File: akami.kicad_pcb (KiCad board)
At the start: 4 copper layers, 30 x 33.3 mm, 66 parts, among them J1 USB_C_Receptacle_USB2.0, J2 Conn_01x01, J3 Conn_01x01, Q2 AO3401A, U1 nRF52840, U2 TP4054, U3 AP2112K-3.3, U4 ProMicro_2, Y1 32MHz, Y2 32.768 kHz

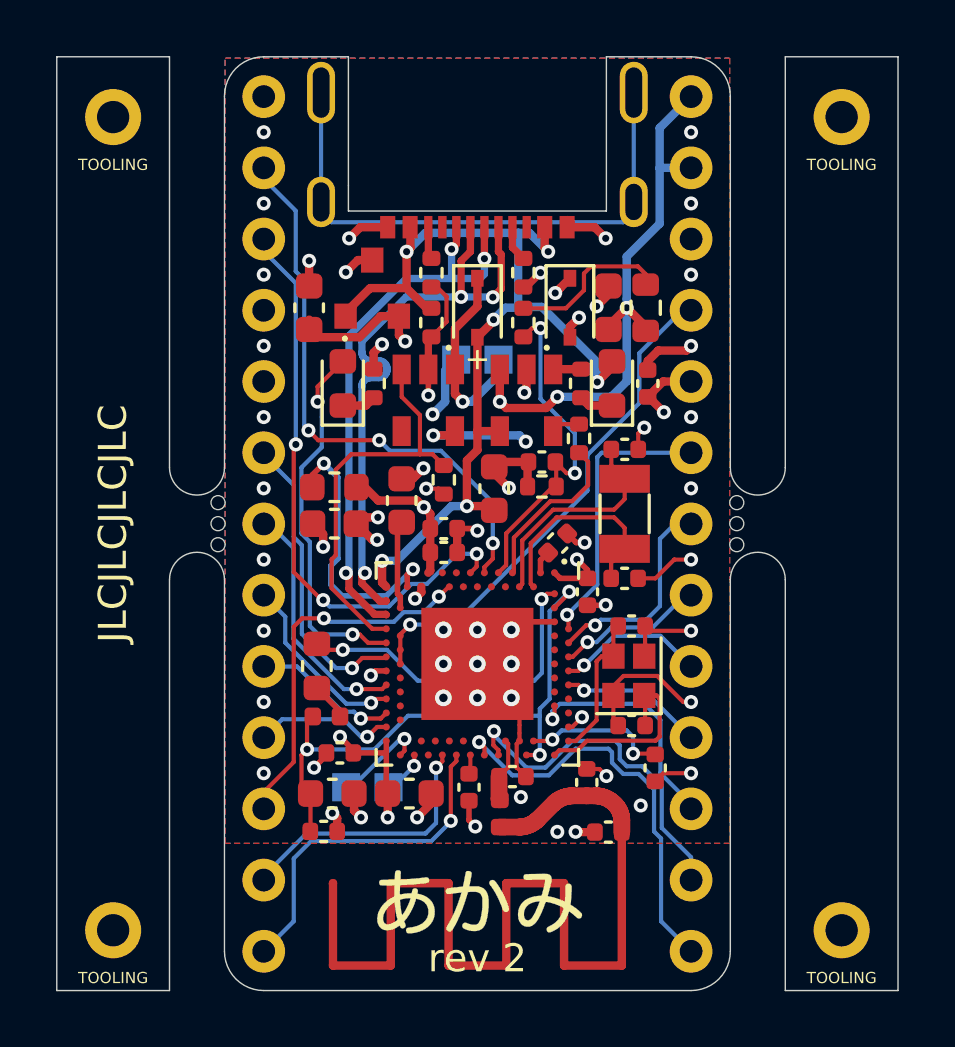
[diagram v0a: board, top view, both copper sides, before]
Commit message: rev 2.1 (hv): 1. remove the 1M pulldown on the LDO enable pin; AP2112K has an    internal pull-down already. 2. adjust pcb layout/routing slightly.
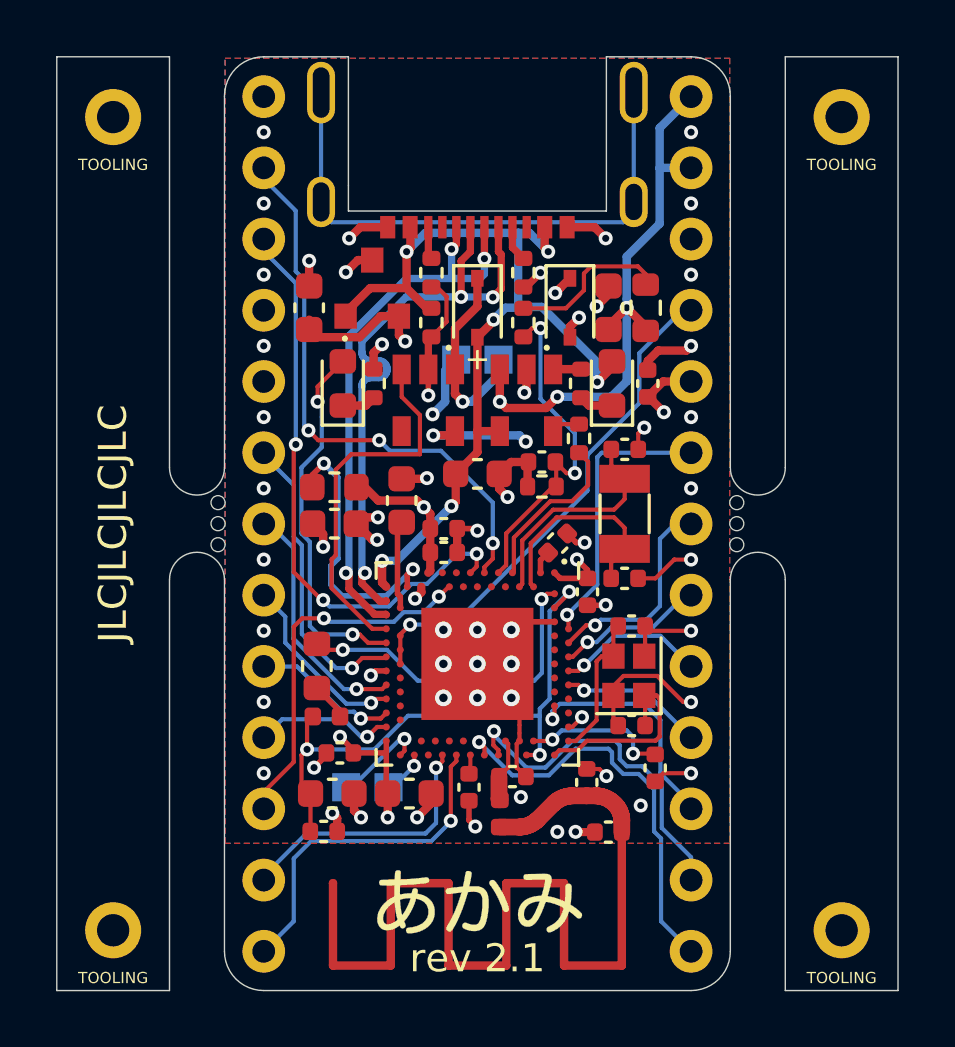
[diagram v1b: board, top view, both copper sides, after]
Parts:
- removed R1: 1M, Resistor_SMD:R_0402_1005Metric
- moved C14 0.80 mm to (0.00, -1.77), turned to 180 degrees
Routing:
- net VBUS: track 35.3 -> 34.0 mm
- net POWER_CTRL: track 14.4 -> 13.4 mm
- net GND: track 43.7 -> 42.8 mm, vias 55 -> 54
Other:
- board text added: "rev 2.1"
- board text removed: "rev 2"

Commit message: rev 2.2 (hv): 1. remove the diode connecting EXT_VCC to VDD_HV; pending further    investigation on how to improve the power path.
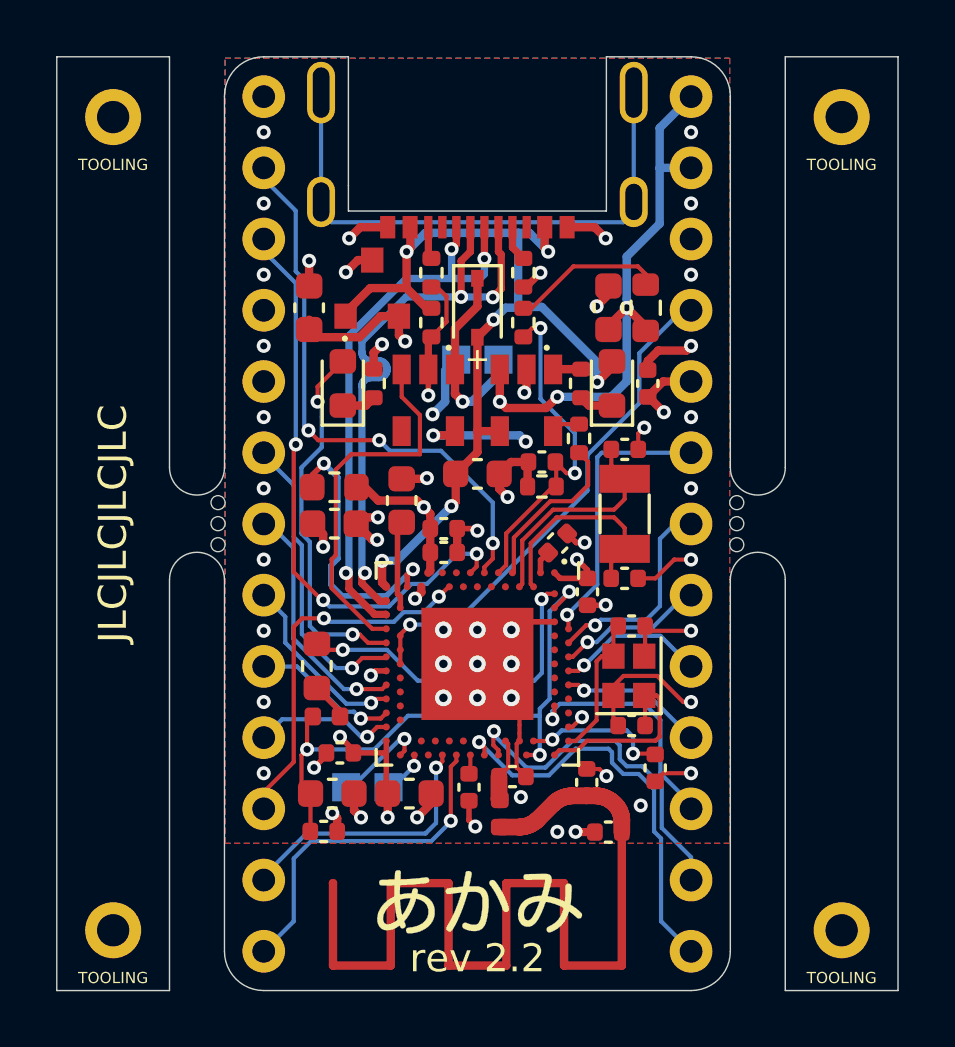
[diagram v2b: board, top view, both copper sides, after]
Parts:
- removed D4: 1N5817, Diode_SMD:D_SOD-323
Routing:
- net VDD_HV: track 35.7 -> 27.1 mm, vias 6 -> 5
- net EXT_VCC: track 16.4 -> 12.2 mm, vias 4 -> 3
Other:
- board text added: "rev 2.2"
- board text removed: "rev 2.1"
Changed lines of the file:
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@@
     (thickness 1.6)
     (drawings 44)
-    (tracks 869)
+    (tracks 853)
     (zones 0)
-    (modules 65)
+    (modules 64)
     (nets 80)
   )
@@
     )
   )
-  (module Diode_SMD:D_SOD-323 (layer F.Cu)
-    (at 3.3 -7.7 270)
-    (descr SOD-323)
-    (tags SOD-323)
-    (attr smd)
-    (fp_text reference D4 (at 0 -0.025 90) (layer Eco2.User)
-      (effects (font (size 0.3 0.3) (thickness 0.05)))
-    )
-    (fp_text value 1N5817 (at 0.1 1.9 90) (layer F.Fab)
-      (effects (font (size 1 1) (thickness 0.15)))
-    )
-    (fp_line (start -1.5 -0.85) (end 1.05 -0.85) (layer F.SilkS) (width 0.12))
-    (fp_line (start -1.5 0.85) (end 1.05 0.85) (layer F.SilkS) (width 0.12))
-    (fp_line (start -1.6 -0.95) (end -1.6 0.95) (layer F.CrtYd) (width 0.05))
-    (fp_line (start -1.6 0.95) (end 1.6 0.95) (layer F.CrtYd) (width 0.05))
-    (fp_line (start 1.6 -0.95) (end 1.6 0.95) (layer F.CrtYd) (width 0.05))
-    (fp_line (start -1.6 -0.95) (end 1.6 -0.95) (layer F.CrtYd) (width 0.05))
-    (fp_line (start -0.9 -0.7) (end 0.9 -0.7) (layer F.Fab) (width 0.1))
-    (fp_line (start 0.9 -0.7) (end 0.9 0.7) (layer F.Fab) (width 0.1))
-    (fp_line (start 0.9 0.7) (end -0.9 0.7) (layer F.Fab) (width 0.1))
-    (fp_line (start -0.9 0.7) (end -0.9 -0.7) (layer F.Fab) (width 0.1))
-    (fp_line (start -0.3 -0.35) (end -0.3 0.35) (layer F.Fab) (width 0.1))
-    (fp_line (start -0.3 0) (end -0.5 0) (layer F.Fab) (width 0.1))
-    (fp_line (start -0.3 0) (end 0.2 -0.35) (layer F.Fab) (width 0.1))
-    (fp_line (start 0.2 -0.35) (end 0.2 0.35) (layer F.Fab) (width 0.1))
-    (fp_line (start 0.2 0.35) (end -0.3 0) (layer F.Fab) (width 0.1))
-    (fp_line (start 0.2 0) (end 0.45 0) (layer F.Fab) (width 0.1))
-    (fp_line (start -1.5 -0.85) (end -1.5 0.85) (layer F.SilkS) (width 0.12))
-    (fp_text user %R (at 0 -1.85 90) (layer F.Fab)
-      (effects (font (size 1 1) (thickness 0.15)))
-    )
-    (pad 1 smd rect (at -1.05 0 270) (size 0.6 0.45) (layers F.Cu F.Paste F.Mask)
-      (net 77 VDD_HV))
-    (pad 2 smd rect (at 1.05 0 270) (size 0.6 0.45) (layers F.Cu F.Paste F.Mask)
-      (net 78 EXT_VCC))
-    (model ${KISYS3DMOD}/Diode_SMD.3dshapes/D_SOD-323.wrl
-      (at (xyz 0 0 0))
-      (scale (xyz 1 1 1))
-      (rotate (xyz 0 0 0))
-    )
-  )
   (module Capacitor_SMD:C_0402_1005Metric (layer F.Cu)
     (at 6.075 -5 90)
@@
     (effects (font (size 0.75 0.75) (thickness 0.13)) (justify mirror))
   )
-  (gr_text "rev 2.1" (at 0 15.5) (layer F.SilkS)
+  (gr_text "rev 2.2" (at 0 15.5) (layer F.SilkS)
     (effects (font (size 1 1) (thickness 0.15)))
   )
@@
   (segment (start -5.2 1.275) (end -5.05 1.125) (width 0.15) (layer F.Cu) (net 26))
   (segment (start -3.25 3.75) (end -3.75 3.75) (width 0.15) (layer F.Cu) (net 26))
-  (segment (start 3.155 -7.68) (end 1.64 -7.68) (width 0.15) (layer F.Cu) (net 27))
-  (segment (start 3.8 -8.325) (end 3.155 -7.68) (width 0.15) (layer F.Cu) (net 27))
-  (segment (start 4.05 -9.175) (end 3.8 -8.925) (width 0.15) (layer F.Cu) (net 27))
-  (segment (start 5.725 -9.175) (end 4.05 -9.175) (width 0.15) (layer F.Cu) (net 27))
-  (segment (start 3.8 -8.925) (end 3.8 -8.325) (width 0.15) (layer F.Cu) (net 27))
+  (segment (start 1.93 -7.68) (end 1.64 -7.68) (width 0.15) (layer F.Cu) (net 27))
+  (segment (start 3.425 -9.175) (end 1.93 -7.68) (width 0.15) (layer F.Cu) (net 27))
+  (segment (start 5.725 -9.175) (end 3.425 -9.175) (width 0.15) (layer F.Cu) (net 27))
   (segment (start 6 -8.9) (end 5.725 -9.175) (width 0.15) (layer F.Cu) (net 27))
   (segment (start 6 -8.525) (end 6 -8.9) (width 0.15) (layer F.Cu) (net 27))
@@
   (segment (start -2 2.45) (end -2.225 2.675) (width 0.3) (layer F.Cu) (net 77))
   (segment (start -2.225 2.675) (end -2.195 2.675) (width 0.3) (layer B.Cu) (net 77))
-  (segment (start -0.35 -2.575) (end 0.625 -3.55) (width 0.3) (layer In2.Cu) (net 77))
-  (segment (start -2.25 -2.575) (end -0.35 -2.575) (width 0.3) (layer In2.Cu) (net 77))
-  (segment (start -2.75 -2.075) (end -2.25 -2.575) (width 0.3) (layer In2.Cu) (net 77))
-  (segment (start -2.75 -1.025) (end -2.75 -2.075) (width 0.3) (layer In2.Cu) (net 77))
-  (segment (start -3.55 -0.225) (end -2.75 -1.025) (width 0.3) (layer In2.Cu) (net 77))
   (via (at -3.55 -0.225) (size 0.5) (drill 0.25) (layers F.Cu B.Cu) (net 77))
   (segment (start -4.1 -0.225) (end -4.325 0) (width 0.3) (layer F.Cu) (net 77))
@@
   (segment (start -2.125 0.575) (end -1.7 1) (width 0.3) (layer In2.Cu) (net 77))
   (segment (start -3.575 0.575) (end -2.125 0.575) (width 0.3) (layer In2.Cu) (net 77))
-  (segment (start -0.175 -4.35) (end 0.625 -3.55) (width 0.3) (layer In2.Cu) (net 77))
-  (segment (start -0.525 -4.35) (end -0.175 -4.35) (width 0.3) (layer In2.Cu) (net 77))
   (segment (start -0.525 -4.45) (end -2.575 -6.5) (width 0.3) (layer In2.Cu) (net 77))
   (segment (start -0.525 -4.35) (end -0.525 -4.45) (width 0.3) (layer In2.Cu) (net 77))
@@
   (segment (start -0.2 -4.35) (end 0.755 -5.305) (width 0.3) (layer B.Cu) (net 77))
   (segment (start -0.525 -4.35) (end -0.2 -4.35) (width 0.3) (layer B.Cu) (net 77))
-  (segment (start 2.775 -8.225) (end 2.95 -8.4) (width 0.3) (layer F.Cu) (net 77))
-  (via (at 2.775 -8.225) (size 0.5) (drill 0.25) (layers F.Cu B.Cu) (net 77))
-  (segment (start 2.775 -8.225) (end 3.3 -8.75) (width 0.3) (layer F.Cu) (net 77))
-  (segment (start 1.425 -3.55) (end 0.625 -3.55) (width 0.3) (layer In2.Cu) (net 77))
-  (segment (start 2.25 -4.375) (end 1.425 -3.55) (width 0.3) (layer In2.Cu) (net 77))
-  (segment (start 2.775 -5.475) (end 2.25 -4.95) (width 0.3) (layer In2.Cu) (net 77))
-  (segment (start 2.25 -4.95) (end 2.25 -4.375) (width 0.3) (layer In2.Cu) (net 77))
-  (segment (start 2.775 -8.225) (end 2.775 -5.475) (width 0.3) (layer In2.Cu) (net 77))
   (segment (start -5.725 -6.65) (end -6 -6.925) (width 0.3) (layer F.Cu) (net 77))
   (segment (start -4.2 -6.65) (end -5.725 -6.65) (width 0.3) (layer F.Cu) (net 77))
   (segment (start -3.45 -7.4) (end -4.2 -6.65) (width 0.3) (layer F.Cu) (net 77))
   (segment (start -2.8 -7.4) (end -3.45 -7.4) (width 0.3) (layer F.Cu) (net 77))
+  (segment (start -0.525 -3.2) (end -0.525 -4.35) (width 0.3) (layer In2.Cu) (net 77))
+  (segment (start -1.15 -2.575) (end -0.525 -3.2) (width 0.3) (layer In2.Cu) (net 77))
+  (segment (start -2.25 -2.575) (end -1.15 -2.575) (width 0.3) (layer In2.Cu) (net 77))
+  (segment (start -2.75 -1.025) (end -2.75 -2.075) (width 0.3) (layer In2.Cu) (net 77))
+  (segment (start -2.75 -2.075) (end -2.25 -2.575) (width 0.3) (layer In2.Cu) (net 77))
+  (segment (start -3.55 -0.225) (end -2.75 -1.025) (width 0.3) (layer In2.Cu) (net 77))
   (via (at 1.725 -2.925) (size 0.5) (drill 0.25) (layers F.Cu B.Cu) (net 78))
   (via (at -1.575 -3.15) (size 0.5) (drill 0.25) (layers F.Cu B.Cu) (net 78))
@@
   (segment (start 2.275 -2.925) (end 3.325 -3.975) (width 0.3) (layer In2.Cu) (net 78))
   (segment (start 1.725 -2.925) (end 2.275 -2.925) (width 0.3) (layer In2.Cu) (net 78))
-  (via (at 3.625 -7.35) (size 0.5) (drill 0.25) (layers F.Cu B.Cu) (net 78))
-  (segment (start 3.3 -7.025) (end 3.625 -7.35) (width 0.3) (layer F.Cu) (net 78))
-  (segment (start 3.3 -6.65) (end 3.3 -7.025) (width 0.3) (layer F.Cu) (net 78))
-  (segment (start 3.625 -4.025) (end 3.675 -3.975) (width 0.3) (layer In2.Cu) (net 78))
-  (segment (start 3.625 -7.35) (end 3.625 -4.025) (width 0.3) (layer In2.Cu) (net 78))
   (segment (start 3.675 -3.975) (end 4.35 -3.975) (width 0.3) (layer In2.Cu) (net 78))
   (segment (start 3.325 -3.975) (end 3.675 -3.975) (width 0.3) (layer In2.Cu) (net 78))

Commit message: rev 2.3 (hv): 1. replace AP2112 LDO with LP5912; it's some weird SMD package but    it's only 2x2mm; 500mA max output and 30uA quiescent. it's not    like we'll be the ones soldering it anyway.
2. similarly, replace 1N5817 schottkys with MSK4010 schottkys; it's
   SOD-523, so even smaller than the 323s.

3. move the components at the top a little further away from the
   USB port, since that has to be hand-soldered.

that freed up a bunch of space to hopefully try some stuff with the
power path.

note: gerbers/BOM/PnP files not updated
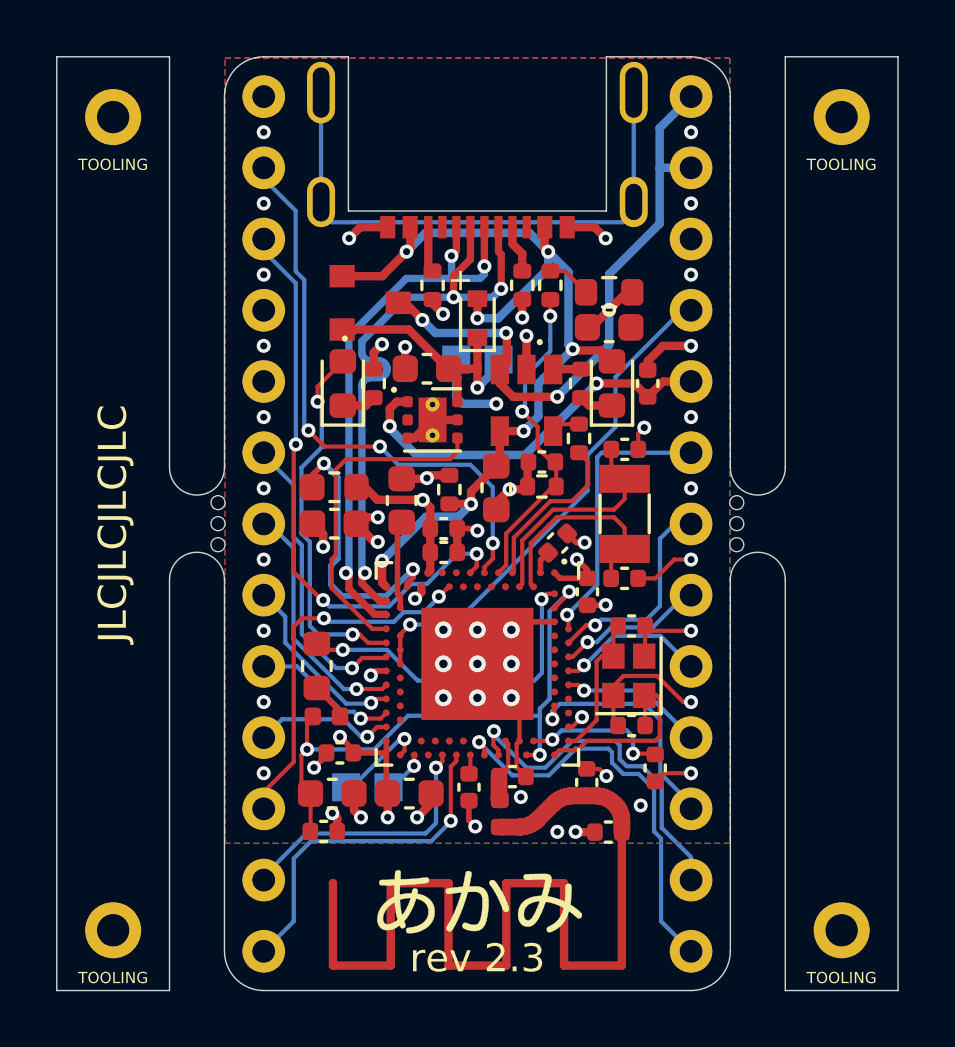
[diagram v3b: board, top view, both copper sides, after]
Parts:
- D2: footprint Diode_SMD:D_SOD-323 -> Diode_SMD:D_SOD-523
- U3: value AP2112K-3.3 -> LP5912-3.3DRV; footprint Package_TO_SOT_SMD:SOT-23-5 -> Package_SON:WSON-6-1EP_2x2mm_P0.65mm_EP1x1.6mm_ThermalVias
- moved R6 5.99 mm to (-1.00, -1.22), turned to 90 degrees
- moved C20 4.73 mm to (-1.80, -5.53), turned to 0 degrees
- moved R3 1.64 mm to (2.60, -8.50)
- moved R11 1.41 mm to (4.70, -8.25), turned to 180 degrees
- moved C14 0.84 mm to (0.68, -1.27), turned to 90 degrees
- moved U3 0.72 mm to (-1.60, -3.70), turned to 0 degrees
- moved C21 0.70 mm to (4.70, -7.00), turned to 180 degrees
- moved Q2 0.53 mm to (-3.83, -7.88), turned to 0 degrees
- moved R10 0.45 mm to (-1.60, -8.50)
- moved R9 0.45 mm to (1.60, -8.50)
- moved D2 0.38 mm to (0.00, -7.33), turned to 90 degrees
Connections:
- U3 pad 1: VDD_HV -> EXT_VCC
- U3 pad 2: GND -> Net-(U3-Pad2)
- U3 pad 3: POWER_CTRL -> GND
- U3 pad 4: Net-(U3-Pad4) -> POWER_CTRL
- U3 pad 5: EXT_VCC -> GND
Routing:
- net VBAT: track 29.1 -> 24.4 mm
- net Net-(R11-Pad2): track 5.47 -> 1.59 mm
- net VDD_HV: track 27.1 -> 23.4 mm, vias 5 -> 4
- net GND: track 42.8 -> 40.5 mm, vias 54 -> 53
- net EXT_VCC: track 12.2 -> 14.1 mm, vias 3 -> 2
- net POWER_CTRL: track 13.4 -> 11.9 mm
- net VDD_NRF: track 15.5 -> 16.2 mm
- net VBUS: track 34.0 -> 33.4 mm, vias 6 -> 7
- net USB_D-: track 22.0 -> 22.6 mm
- net BAT_VOLT: track 12.2 -> 11.6 mm
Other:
- board text added: "rev 2.3"
- board text removed: "rev 2.2"
